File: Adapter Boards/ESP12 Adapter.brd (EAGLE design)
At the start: 29.2 x 24.1 mm, 5 parts, among them U1 WI07-12FULL

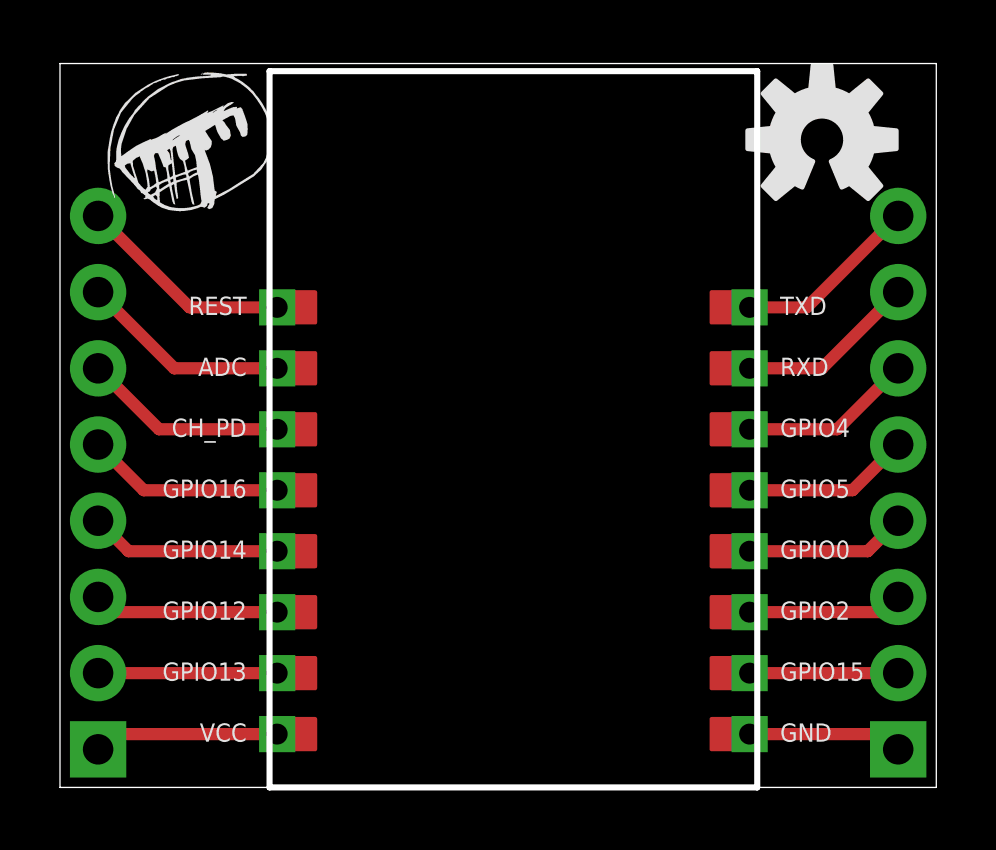
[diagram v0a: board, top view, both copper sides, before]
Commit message: Repair pads; resize ESP12
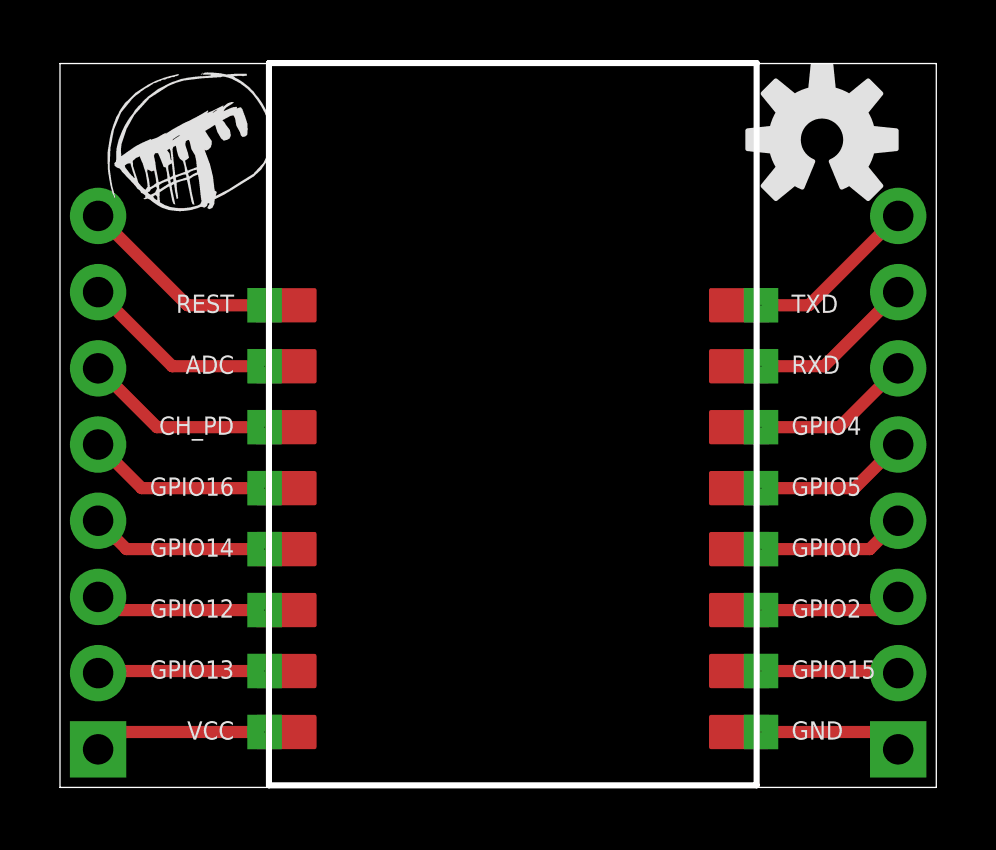
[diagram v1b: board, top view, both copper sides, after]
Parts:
- U1: value WI07-12FULL -> ESP12; device ESP:WI07-12 -> ESP:ESP12
- moved U1 24.1 mm to (6.99, 24.1)
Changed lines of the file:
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@@
 </element>
 <element name="U$1" library="SparkFun-Aesthetics" package="OSHW-LOGO-M" value="" x="25.4" y="21.59"/>
-<element name="U1" library="ESP" package="WI07-12" value="WI07-12FULL" x="6.985" y="0"/>
 <element name="U$2" library="ESP" package="HARK-S" value="" x="1.27" y="19.05"/>
+<element name="U1" library="ESP" package="ESP12" value="ESP12" x="6.985" y="24.13"/>
 </elements>
 <signals>
@@
 <contactref element="JP1" pad="1"/>
 <contactref element="U1" pad="VCC"/>
-<wire x1="7.239" y1="1.778" x2="1.778" y2="1.778" width="0.4064" layer="1"/>
-<wire x1="1.778" y1="1.778" x2="1.27" y2="1.27" width="0.4064" layer="1"/>
+<wire x1="6.819" y1="1.848" x2="1.848" y2="1.848" width="0.4064" layer="1"/>
+<wire x1="1.848" y1="1.848" x2="1.27" y2="1.27" width="0.4064" layer="1"/>
 </signal>
 <signal name="N$2">
 <contactref element="JP1" pad="2"/>
 <contactref element="U1" pad="GPIO13"/>
-<wire x1="7.239" y1="3.81" x2="1.27" y2="3.81" width="0.4064" layer="1"/>
+<wire x1="6.819" y1="3.88" x2="1.34" y2="3.88" width="0.4064" layer="1"/>
+<wire x1="1.34" y1="3.88" x2="1.27" y2="3.81" width="0.4064" layer="1"/>
 </signal>
 <signal name="N$3">
 <contactref element="JP1" pad="3"/>
 <contactref element="U1" pad="GPIO12"/>
-<wire x1="7.239" y1="5.842" x2="1.778" y2="5.842" width="0.4064" layer="1"/>
-<wire x1="1.778" y1="5.842" x2="1.27" y2="6.35" width="0.4064" layer="1"/>
+<wire x1="6.819" y1="5.912" x2="1.708" y2="5.912" width="0.4064" layer="1"/>
+<wire x1="1.708" y1="5.912" x2="1.27" y2="6.35" width="0.4064" layer="1"/>
 </signal>
 <signal name="N$4">
 <contactref element="JP1" pad="4"/>
 <contactref element="U1" pad="GPIO14"/>
-<wire x1="7.239" y1="7.874" x2="2.286" y2="7.874" width="0.4064" layer="1"/>
-<wire x1="2.286" y1="7.874" x2="1.27" y2="8.89" width="0.4064" layer="1"/>
+<wire x1="6.819" y1="7.944" x2="2.216" y2="7.944" width="0.4064" layer="1"/>
+<wire x1="2.216" y1="7.944" x2="1.27" y2="8.89" width="0.4064" layer="1"/>
 </signal>
 <signal name="N$5">
 <contactref element="JP1" pad="5"/>
 <contactref element="U1" pad="GPIO16"/>
-<wire x1="7.239" y1="9.906" x2="2.794" y2="9.906" width="0.4064" layer="1"/>
-<wire x1="2.794" y1="9.906" x2="1.27" y2="11.43" width="0.4064" layer="1"/>
+<wire x1="6.819" y1="9.976" x2="2.724" y2="9.976" width="0.4064" layer="1"/>
+<wire x1="2.724" y1="9.976" x2="1.27" y2="11.43" width="0.4064" layer="1"/>
 </signal>
 <signal name="N$6">
 <contactref element="JP1" pad="6"/>
 <contactref element="U1" pad="CH_PD"/>
-<wire x1="7.239" y1="11.938" x2="3.302" y2="11.938" width="0.4064" layer="1"/>
-<wire x1="3.302" y1="11.938" x2="1.27" y2="13.97" width="0.4064" layer="1"/>
+<wire x1="6.819" y1="12.008" x2="3.232" y2="12.008" width="0.4064" layer="1"/>
+<wire x1="3.232" y1="12.008" x2="1.27" y2="13.97" width="0.4064" layer="1"/>
 </signal>
 <signal name="N$7">
 <contactref element="JP1" pad="7"/>
 <contactref element="U1" pad="ADC"/>
-<wire x1="7.239" y1="13.97" x2="3.81" y2="13.97" width="0.4064" layer="1"/>
-<wire x1="3.81" y1="13.97" x2="1.27" y2="16.51" width="0.4064" layer="1"/>
+<wire x1="6.819" y1="14.04" x2="3.74" y2="14.04" width="0.4064" layer="1"/>
+<wire x1="3.74" y1="14.04" x2="1.27" y2="16.51" width="0.4064" layer="1"/>
 </signal>
 <signal name="N$8">
 <contactref element="JP1" pad="8"/>
 <contactref element="U1" pad="REST"/>
-<wire x1="7.239" y1="16.002" x2="4.318" y2="16.002" width="0.4064" layer="1"/>
-<wire x1="4.318" y1="16.002" x2="1.27" y2="19.05" width="0.4064" layer="1"/>
+<wire x1="6.819" y1="16.072" x2="4.248" y2="16.072" width="0.4064" layer="1"/>
+<wire x1="4.248" y1="16.072" x2="1.27" y2="19.05" width="0.4064" layer="1"/>
 </signal>
 <signal name="N$9">
 <contactref element="JP2" pad="8"/>
 <contactref element="U1" pad="TXD"/>
-<wire x1="22.987" y1="16.002" x2="24.892" y2="16.002" width="0.4064" layer="1"/>
-<wire x1="24.892" y1="16.002" x2="27.94" y2="19.05" width="0.4064" layer="1"/>
+<wire x1="23.367" y1="16.072" x2="24.962" y2="16.072" width="0.4064" layer="1"/>
+<wire x1="24.962" y1="16.072" x2="27.94" y2="19.05" width="0.4064" layer="1"/>
 </signal>
 <signal name="N$10">
 <contactref element="JP2" pad="7"/>
 <contactref element="U1" pad="RXD"/>
-<wire x1="22.987" y1="13.97" x2="25.4" y2="13.97" width="0.4064" layer="1"/>
-<wire x1="25.4" y1="13.97" x2="27.94" y2="16.51" width="0.4064" layer="1"/>
+<wire x1="23.367" y1="14.04" x2="25.47" y2="14.04" width="0.4064" layer="1"/>
+<wire x1="25.47" y1="14.04" x2="27.94" y2="16.51" width="0.4064" layer="1"/>
 </signal>
 <signal name="N$11">
 <contactref element="JP2" pad="6"/>
 <contactref element="U1" pad="GPIO4"/>
-<wire x1="22.987" y1="11.938" x2="25.908" y2="11.938" width="0.4064" layer="1"/>
-<wire x1="25.908" y1="11.938" x2="27.94" y2="13.97" width="0.4064" layer="1"/>
+<wire x1="23.367" y1="12.008" x2="25.978" y2="12.008" width="0.4064" layer="1"/>
+<wire x1="25.978" y1="12.008" x2="27.94" y2="13.97" width="0.4064" layer="1"/>
 </signal>
 <signal name="N$12">
 <contactref element="JP2" pad="5"/>
 <contactref element="U1" pad="GPIO5"/>
-<wire x1="22.987" y1="9.906" x2="26.416" y2="9.906" width="0.4064" layer="1"/>
-<wire x1="26.416" y1="9.906" x2="27.94" y2="11.43" width="0.4064" layer="1"/>
+<wire x1="23.367" y1="9.976" x2="26.486" y2="9.976" width="0.4064" layer="1"/>
+<wire x1="26.486" y1="9.976" x2="27.94" y2="11.43" width="0.4064" layer="1"/>
 </signal>
 <signal name="N$13">
 <contactref element="JP2" pad="4"/>
 <contactref element="U1" pad="GPIO0"/>
-<wire x1="22.987" y1="7.874" x2="26.924" y2="7.874" width="0.4064" layer="1"/>
-<wire x1="26.924" y1="7.874" x2="27.94" y2="8.89" width="0.4064" layer="1"/>
+<wire x1="23.367" y1="7.944" x2="26.994" y2="7.944" width="0.4064" layer="1"/>
+<wire x1="26.994" y1="7.944" x2="27.94" y2="8.89" width="0.4064" layer="1"/>
 </signal>
 <signal name="N$14">
 <contactref element="JP2" pad="3"/>
 <contactref element="U1" pad="GPIO2"/>
-<wire x1="22.987" y1="5.842" x2="27.432" y2="5.842" width="0.4064" layer="1"/>
-<wire x1="27.432" y1="5.842" x2="27.94" y2="6.35" width="0.4064" layer="1"/>
+<wire x1="23.367" y1="5.912" x2="27.502" y2="5.912" width="0.4064" layer="1"/>
+<wire x1="27.502" y1="5.912" x2="27.94" y2="6.35" width="0.4064" layer="1"/>
 </signal>
 <signal name="N$15">
 <contactref element="JP2" pad="2"/>
 <contactref element="U1" pad="GPIO15"/>
-<wire x1="22.987" y1="3.81" x2="27.94" y2="3.81" width="0.4064" layer="1"/>
+<wire x1="23.367" y1="3.88" x2="27.87" y2="3.88" width="0.4064" layer="1"/>
+<wire x1="27.87" y1="3.88" x2="27.94" y2="3.81" width="0.4064" layer="1"/>
 </signal>
 <signal name="N$16">
 <contactref element="JP2" pad="1"/>
 <contactref element="U1" pad="GND"/>
-<wire x1="22.987" y1="1.778" x2="27.432" y2="1.778" width="0.4064" layer="1"/>
-<wire x1="27.432" y1="1.778" x2="27.94" y2="1.27" width="0.4064" layer="1"/>
+<wire x1="23.367" y1="1.848" x2="27.362" y2="1.848" width="0.4064" layer="1"/>
+<wire x1="27.362" y1="1.848" x2="27.94" y2="1.27" width="0.4064" layer="1"/>
 </signal>
 </signals>
